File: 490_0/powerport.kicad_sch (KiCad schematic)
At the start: 8 parts, among them J10 TS-103-G-A, J9 2171790001, U5 TS3USB221AQRSERQ1

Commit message: finished BOM
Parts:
- C23: Digikey Link (none) -> https://www.digikey.ca/en/products/detail/samsung-electro-m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; Manufacturer (none) -> Samsung Electro-Mechanics; Manufacturer Part (none) -> CL31B226KPHNNNE; Package (none) -> 1206 (3216 Metric); Price (none) -> 0.39; Supplier (none) -> DigiKey; Supplier P/N (none) -> 1276-2769-1-ND; Type (none) -> SMD; Unit (none) -> pcs
- C28: Digikey Link (none) -> https://www.digikey.ca/en/products/detail/samsung-electro-m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; Manufacturer (none) -> Samsung Electro-Mechanics; Manufacturer Part (none) -> CL31B104KBCNNNC; Package (none) -> 1206 (3216 Metric); Price (none) -> 0.11; Supplier (none) -> DigiKey; Supplier P/N (none) -> 1276-1017-1-ND; Type (none) -> SMD, MLCC; Unit (none) -> pcs
- J10: footprint S2B-XH-A:JST_S2B-XH-A -> (none); Digikey Link (none) -> https://www.digikey.ca/en/products/detail/samtec-inc/TS-103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; Manufacturer (none) -> Samtec Inc.; Manufacturer Part (none) -> TS-103-G-A; Price (none) -> 1.27; Supplier (none) -> DigiKey; Supplier P/N (none) -> SAM1111-03-ND; Type (none) -> Through Hole; Unit (none) -> pcs
- R18, R19: Digikey Link (none) -> https://www.digikey.ca/en/products/detail/yageo/RC1206FR-07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; Manufacturer (none) -> YAGEO; Manufacturer Part (none) -> RC1206FR-075K1L; Package (none) -> 1206; Price (none) -> 0.1; Supplier (none) -> DigiKey; Supplier P/N (none) -> 311-5.10KFRCT-ND; Type (none) -> SMD; Unit (none) -> pcs

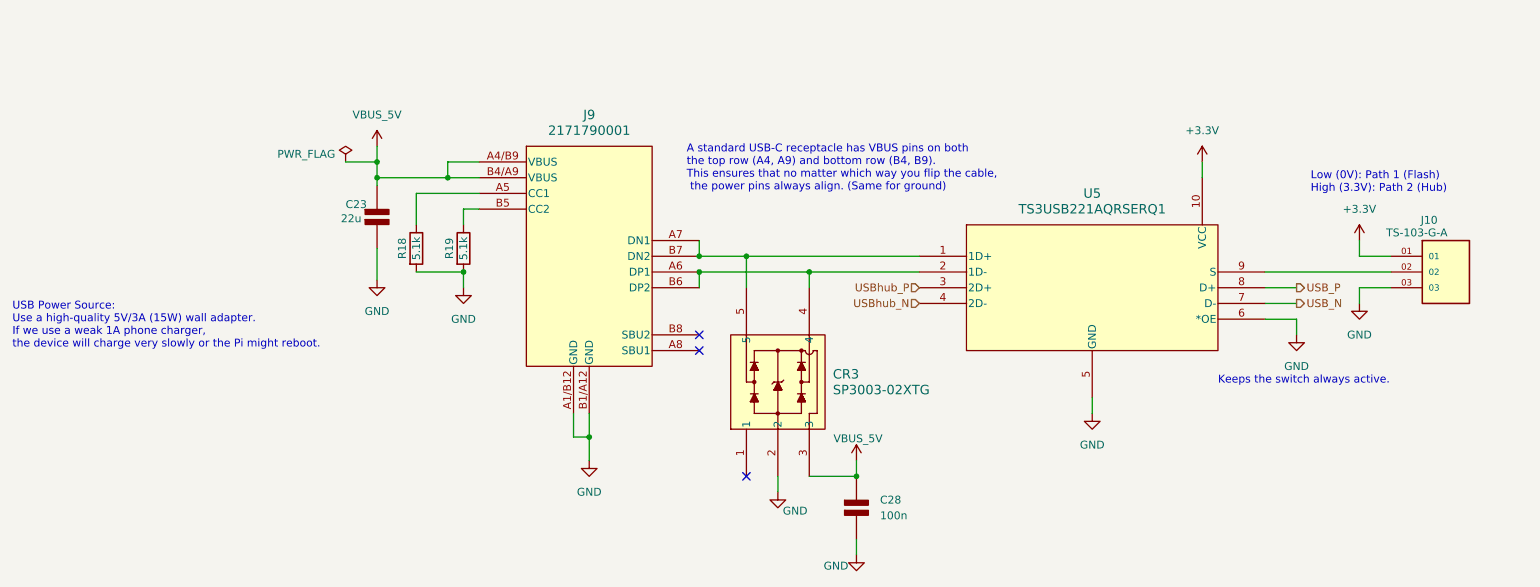
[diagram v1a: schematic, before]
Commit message: Implemented Dmitry comments
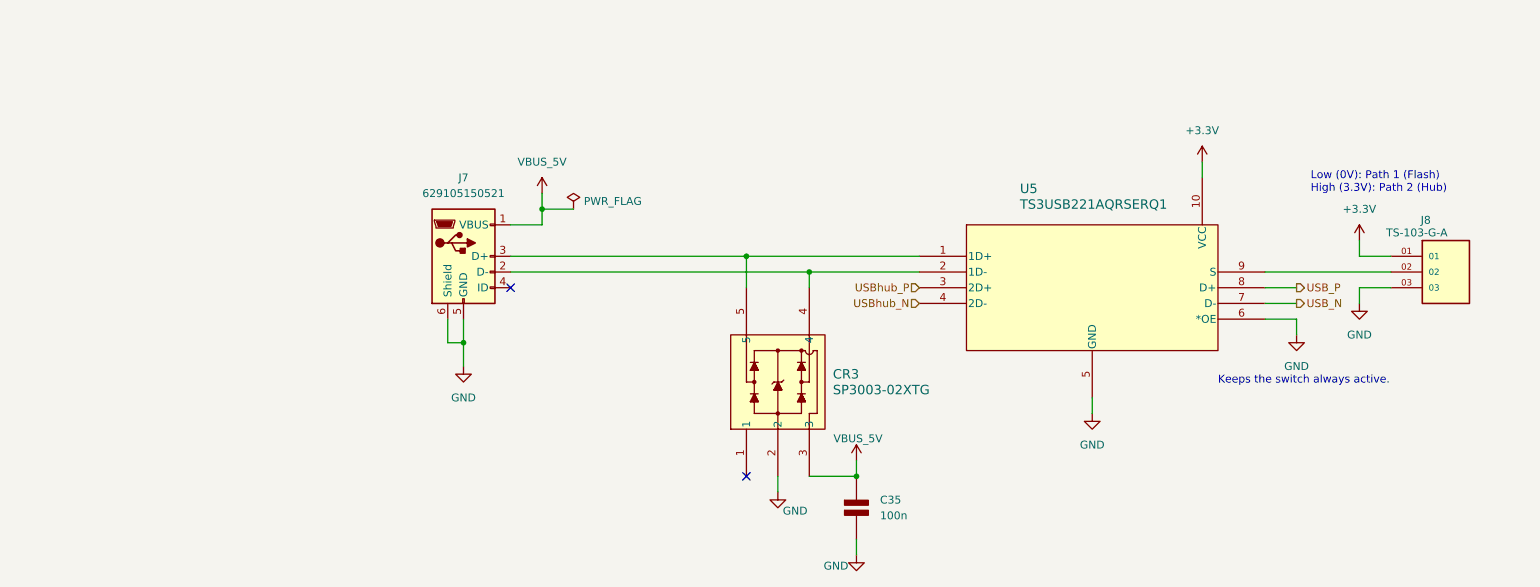
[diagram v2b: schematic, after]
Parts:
- removed C23: 22u, symbol PCM_Elektuur:C
- removed J9: 2171790001, S2B-XH-A:JST_S2B-XH-A, symbol capstone_parts:2171790001
- removed R18, R19: 5.1k, symbol Device:R
- added J7: 629105150521, symbol Connector:USB_B_Micro
- renumbered C28 to C35, J10 to J8
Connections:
- net GND: now also J7.5 (GND), J7.6 (Shield)
- net VBUS_5V: now also J7.1 (VBUS)
- net at CR3.5, U5.1 (1D+): now also J7.3 (D+)
- net at CR3.4, U5.2 (1D-): now also J7.2 (D-)
- no-connect marks 3 -> 2
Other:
- note removed: "A standard USB-C receptacle has VBUS pins on both the top row (A4, A9) and bottom row (B4, B9). This ensures that no matter which way you flip the cable, the power pins always align. (Same for ground)"
- note removed: "USB Power Source: Use a high-quality 5V/3A (15W) wall adapter. If we use a weak 1A phone charger, the device will charge very slowly or the Pi might reboot."

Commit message: Final Fixes
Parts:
- renumbered C35 to C29
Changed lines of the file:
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@@
 		(on_board yes)
 		(dnp no)
-		(property "Reference" "#PWR066"
+		(property "Reference" "#PWR058"
 			(at 210.82 72.39 0)
 			(effects
@@
 			(project "490_0"
 				(path "/365a82ed-827d-43e1-aa2f-b98221c4179c/f9f22bb2-829e-4ff5-89be-c4b5e2122135/d28f2748-3083-434f-ab92-5f07809e59a3"
-					(reference "#PWR066")
+					(reference "#PWR058")
 					(unit 1)
 				)
@@
 		(on_board yes)
 		(dnp no)
-		(property "Reference" "#PWR082"
+		(property "Reference" "#PWR074"
 			(at 142.24 128.27 0)
 			(effects
@@
 			(project "490_0"
 				(path "/365a82ed-827d-43e1-aa2f-b98221c4179c/f9f22bb2-829e-4ff5-89be-c4b5e2122135/d28f2748-3083-434f-ab92-5f07809e59a3"
-					(reference "#PWR082")
+					(reference "#PWR074")
 					(unit 1)
 				)
@@
 		(dnp no)
 		(fields_autoplaced yes)
-		(property "Reference" "#PWR067"
+		(property "Reference" "#PWR059"
 			(at 104.14 77.47 0)
 			(effects
@@
 			(project "490_0"
 				(path "/365a82ed-827d-43e1-aa2f-b98221c4179c/f9f22bb2-829e-4ff5-89be-c4b5e2122135/d28f2748-3083-434f-ab92-5f07809e59a3"
-					(reference "#PWR067")
+					(reference "#PWR059")
 					(unit 1)
 				)
@@
 		(dnp no)
 		(fields_autoplaced yes)
-		(property "Reference" "#PWR076"
+		(property "Reference" "#PWR068"
 			(at 226.06 102.87 0)
 			(effects
@@
 			(project "490_0"
 				(path "/365a82ed-827d-43e1-aa2f-b98221c4179c/f9f22bb2-829e-4ff5-89be-c4b5e2122135/d28f2748-3083-434f-ab92-5f07809e59a3"
-					(reference "#PWR076")
+					(reference "#PWR068")
 					(unit 1)
 				)
@@
 		(dnp no)
 		(fields_autoplaced yes)
-		(property "Reference" "#PWR077"
+		(property "Reference" "#PWR069"
 			(at 91.44 107.95 0)
 			(effects
@@
 			(project "490_0"
 				(path "/365a82ed-827d-43e1-aa2f-b98221c4179c/f9f22bb2-829e-4ff5-89be-c4b5e2122135/d28f2748-3083-434f-ab92-5f07809e59a3"
-					(reference "#PWR077")
+					(reference "#PWR069")
 					(unit 1)
 				)
@@
 		(dnp no)
 		(fields_autoplaced yes)
-		(property "Reference" "#PWR075"
+		(property "Reference" "#PWR067"
 			(at 236.22 97.79 0)
 			(effects
@@
 			(project "490_0"
 				(path "/365a82ed-827d-43e1-aa2f-b98221c4179c/f9f22bb2-829e-4ff5-89be-c4b5e2122135/d28f2748-3083-434f-ab92-5f07809e59a3"
-					(reference "#PWR075")
+					(reference "#PWR067")
 					(unit 1)
 				)
@@
 		(dnp no)
 		(fields_autoplaced yes)
-		(property "Reference" "#PWR078"
+		(property "Reference" "#PWR070"
 			(at 193.04 115.57 0)
 			(effects
@@
 			(project "490_0"
 				(path "/365a82ed-827d-43e1-aa2f-b98221c4179c/f9f22bb2-829e-4ff5-89be-c4b5e2122135/d28f2748-3083-434f-ab92-5f07809e59a3"
-					(reference "#PWR078")
+					(reference "#PWR070")
 					(unit 1)
 				)
@@
 		(on_board yes)
 		(dnp no)
-		(property "Reference" "#PWR084"
+		(property "Reference" "#PWR076"
 			(at 154.94 138.43 0)
 			(effects
@@
 			(project "490_0"
 				(path "/365a82ed-827d-43e1-aa2f-b98221c4179c/f9f22bb2-829e-4ff5-89be-c4b5e2122135/d28f2748-3083-434f-ab92-5f07809e59a3"
-					(reference "#PWR084")
+					(reference "#PWR076")
 					(unit 1)
 				)
@@
 		(on_board yes)
 		(dnp no)
-		(property "Reference" "#PWR080"
+		(property "Reference" "#PWR072"
 			(at 154.94 120.65 0)
 			(effects
@@
 			(project "490_0"
 				(path "/365a82ed-827d-43e1-aa2f-b98221c4179c/f9f22bb2-829e-4ff5-89be-c4b5e2122135/d28f2748-3083-434f-ab92-5f07809e59a3"
-					(reference "#PWR080")
+					(reference "#PWR072")
 					(unit 1)
 				)
@@
 		(on_board yes)
 		(dnp no)
-		(property "Reference" "C35"
+		(property "Reference" "C29"
 			(at 158.75 123.1899 0)
 			(effects
@@
 			(project "490_0"
 				(path "/365a82ed-827d-43e1-aa2f-b98221c4179c/f9f22bb2-829e-4ff5-89be-c4b5e2122135/d28f2748-3083-434f-ab92-5f07809e59a3"
-					(reference "C35")
+					(reference "C29")
 					(unit 1)
 				)
@@
 		(on_board yes)
 		(dnp no)
-		(property "Reference" "#PWR070"
+		(property "Reference" "#PWR062"
 			(at 236.22 85.09 0)
 			(effects
@@
 			(project "490_0"
 				(path "/365a82ed-827d-43e1-aa2f-b98221c4179c/f9f22bb2-829e-4ff5-89be-c4b5e2122135/d28f2748-3083-434f-ab92-5f07809e59a3"
-					(reference "#PWR070")
+					(reference "#PWR062")
 					(unit 1)
 				)

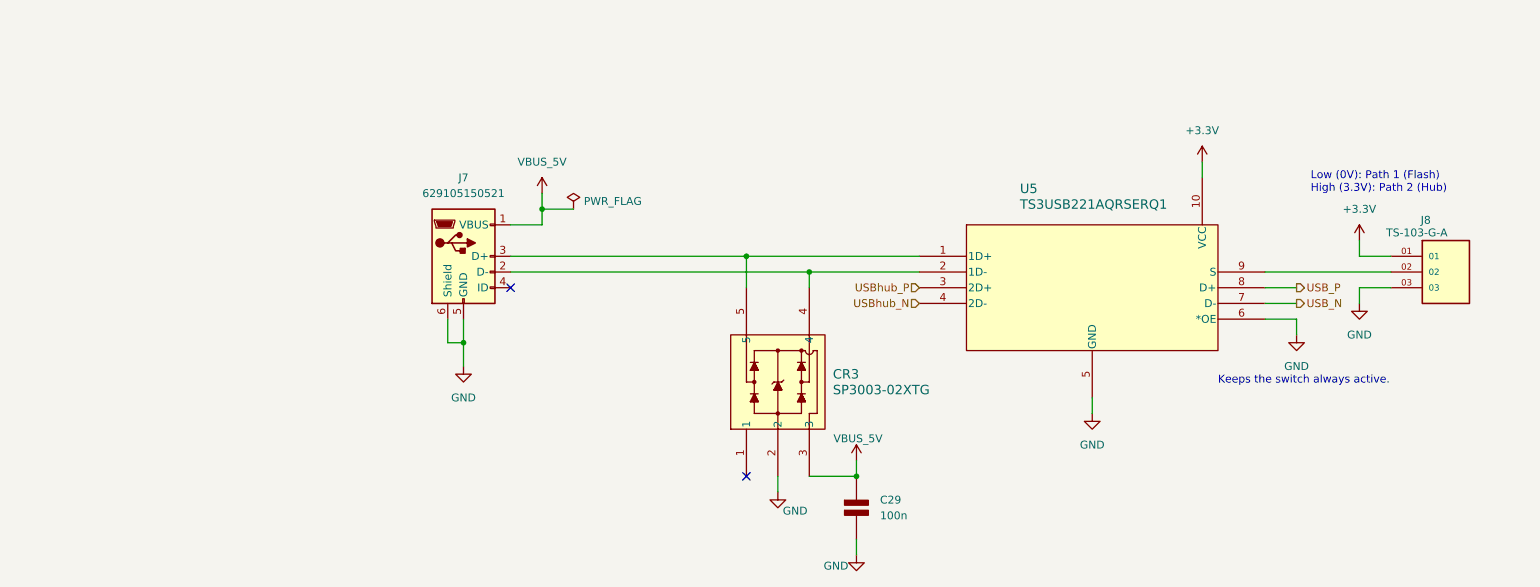
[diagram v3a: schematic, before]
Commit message: Implemented suggestions
notes on schematics:
Overall: Schematics needs to be improved, more compact and cleaner
=========================
I) on root page (page 1):
overall: needs a bit of clean up of the diagram

1. the diagram shows pcb3 and pcb1, but no pcb2, it is probably outdated and therefore might have errors in it, fix it to the latest version and rename things to reflect what it actually is. Also try to clean it up a bit
2. The PCB-3 seem to have the cameras directly connected to the usb hub, how will this be connected? with connectors? if so add them to the diagram, if it's with wires soldered directly to the pcb, try to make note of it for clarity
4. for some reason your TOF is above PCB-3 but is only connected to PCB1, will the TOF be on the glasses, or will you be moving this to the main board? maybe have TOF on the chest for depth, and 2 cameras on glasses for vision, it will also reduce length of cable, which is ideal, i don't think it will work if you run it from the glasses to pcb1 though.
I know, this is a problem, we discussed the chest thing, the problem is the length of the cable but also the haptic feedback is weird if they turn their head.
5. Rename PCB1/PCB3 to PCB1 (chest) PCB3 (glasses) for clarity. Also i don't think (mayeb i'm wrong) that the 5 conected buttons should be on a bus, a bus implies that multiple devices communicate on the same single line. You're using individual lines for each to individual gpio, no?

=========================
II) on PCB-3 usb 2.0 bridge page (page 10)
overall: check datasheet and make sure you've done the connection right and values are selected properly, with the chip data lines properly pulled up/down whether externally or internally. This is important

1. C3/C11 are the input capacitors to U2/u3 TPS553DBVR, datasheet says 100nF, you used 10uF, why? stick to 100nF
2. you seem to have implemented one of /Uthe typical application circuit, look at the others. You have on page 21 of datasheet an auto-retry wi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
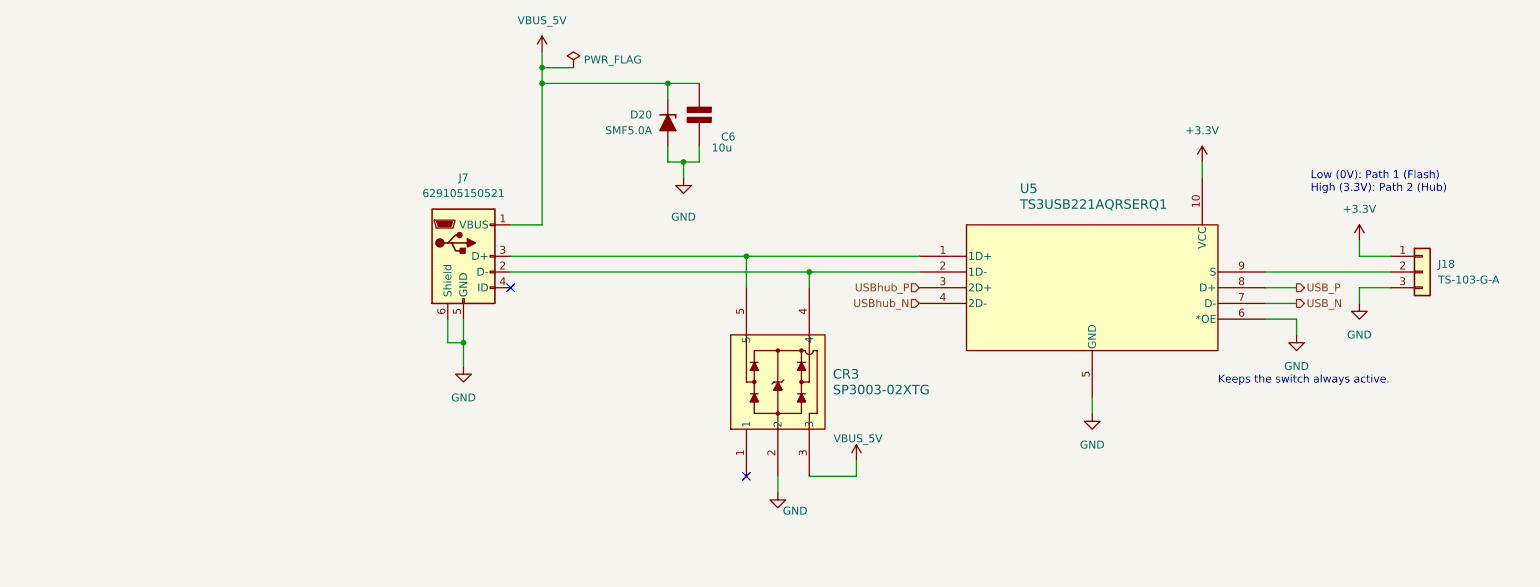
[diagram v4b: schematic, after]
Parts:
- removed C29: 100n, symbol PCM_Elektuur:C
- removed J8: TS-103-G-A, symbol capstone_parts:TS-103-G-A
- added C6: 10u, symbol PCM_Elektuur:C
- added D20: SMF5.0A, PCM_Diode_SMD_AKL:D_SOD-123F, symbol PCM_Diode_TVS_AKL:SMF5.0A
- added J18: TS-103-G-A, 4ms_Connector:Pins_1x03_2.54mm_TH_AudioInsRGndL, symbol PCM_4ms_Connector:Conn_01x03
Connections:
- net +3.3V: now also J18.1 (Pin_1)
- net GND: now also C6.2 (-), D20.2 (A), J18.3 (Pin_3)
- net VBUS_5V: now also C6.1 (+), D20.1 (K)
- net at U5.9 (S): now also J18.2 (Pin_2)

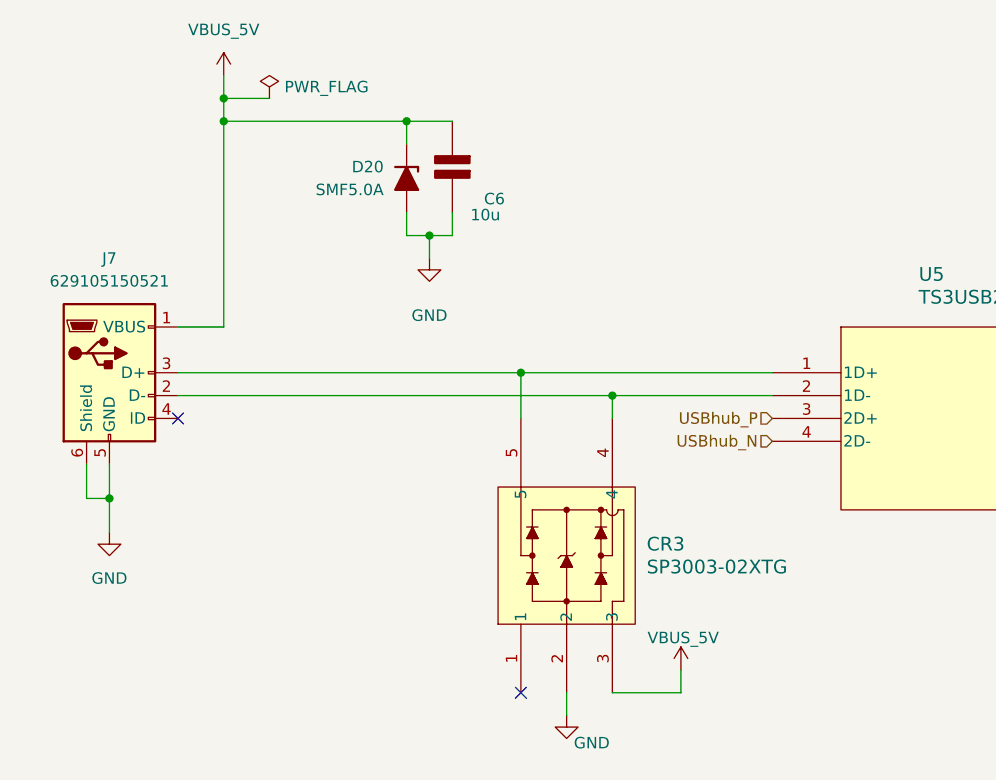
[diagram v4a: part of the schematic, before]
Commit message: FFC to HDMI change
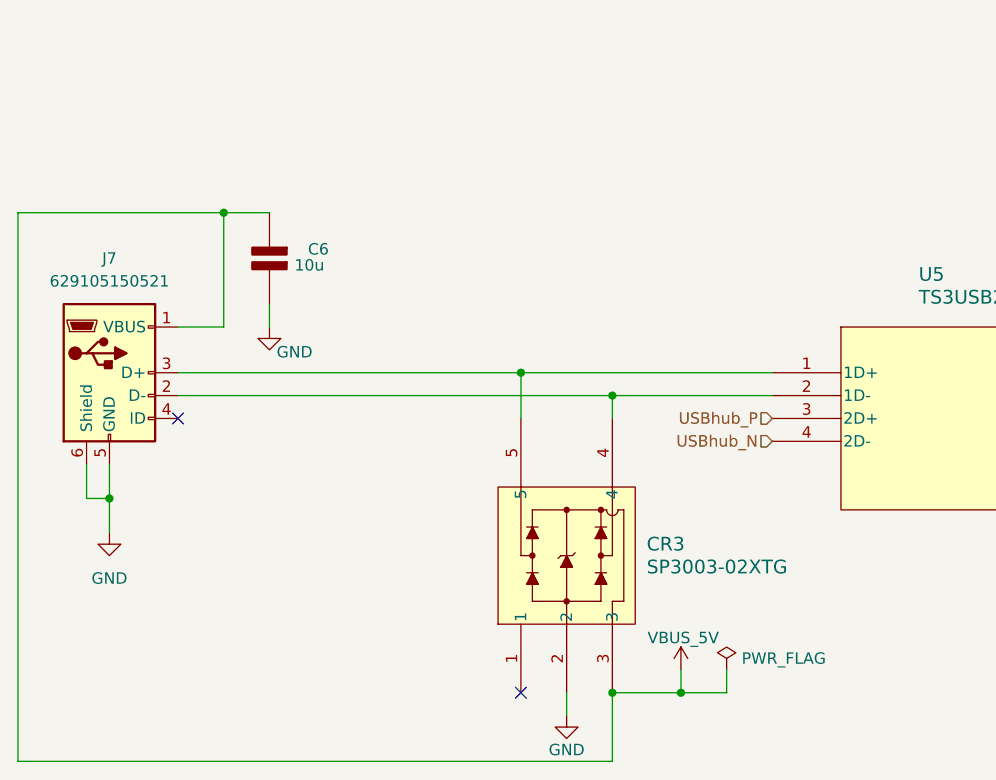
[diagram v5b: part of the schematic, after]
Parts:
- removed D20: SMF5.0A, PCM_Diode_SMD_AKL:D_SOD-123F, symbol PCM_Diode_TVS_AKL:SMF5.0A
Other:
- moved on the sheet: C6

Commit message: Footprint Update
1st half of footprints updated
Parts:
- CR3: footprint (none) -> *CapStone*:SOT553_LTF_SP3003_02XTG
- J18: footprint 4ms_Connector:Pins_1x03_2.54mm_TH_AudioInsRGndL -> *CapStone*:CON3_1X3_TU_HTS_SAI - 3POS Connector
- J7: footprint (none) -> Connector_USB:USB_Micro-B_Wuerth_629105150521
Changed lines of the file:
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@@
 			)
 		)
-		(property "Footprint" "4ms_Connector:Pins_1x03_2.54mm_TH_AudioInsRGndL"
+		(property "Footprint" "*CapStone*:CON3_1X3_TU_HTS_SAI - 3POS Connector"
 			(at 246.38 79.375 0)
 			(effects
@@
 			)
 		)
-		(property "Footprint" ""
+		(property "Footprint" "Connector_USB:USB_Micro-B_Wuerth_629105150521"
 			(at 95.25 85.09 0)
 			(effects
@@
 			)
 		)
-		(property "Footprint" ""
+		(property "Footprint" "*CapStone*:SOT553_LTF_SP3003_02XTG"
 			(at 137.16 119.38 0)
 			(effects

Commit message: Footprint Update #2
All footprints except for the capacitors have been attributed
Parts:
- U5: footprint PCA9685:TSSOP28 -> *CapStone*:RSE10
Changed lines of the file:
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@@
 			)
 		)
-		(property "Footprint" "PCA9685:TSSOP28"
+		(property "Footprint" "*CapStone*:RSE10"
 			(at 165.1 83.82 0)
 			(effects

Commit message: Changed 8conn and BOM update
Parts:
- C6: footprint (none) -> Capacitor_SMD:C_1206_3216Metric
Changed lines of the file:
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@@
 			)
 		)
-		(property "Footprint" ""
+		(property "Footprint" "Capacitor_SMD:C_1206_3216Metric"
 			(at 109.22 71.12 0)
 			(effects
